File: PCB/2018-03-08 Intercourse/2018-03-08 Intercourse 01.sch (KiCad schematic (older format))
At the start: 47 parts, among them J1 USB_C_Receptacle, J2 TP_RST, J3 TP_TX, J4 TP_RX, J5 TP_GPIO0, J6 TP_GND1, J7 TP_GND2, J8 TP_GND3, U1 LTC3225, U2 TPS61221DCKR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

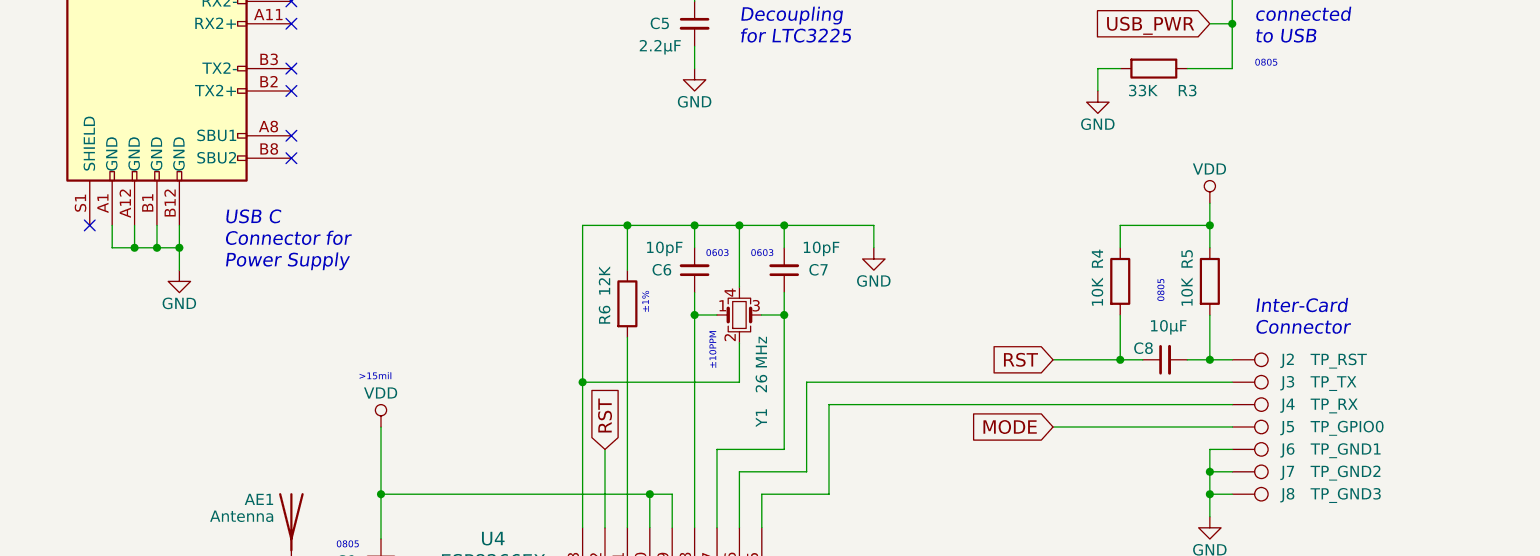
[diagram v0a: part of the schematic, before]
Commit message: Add USBRST Connection on .sch & .pcb
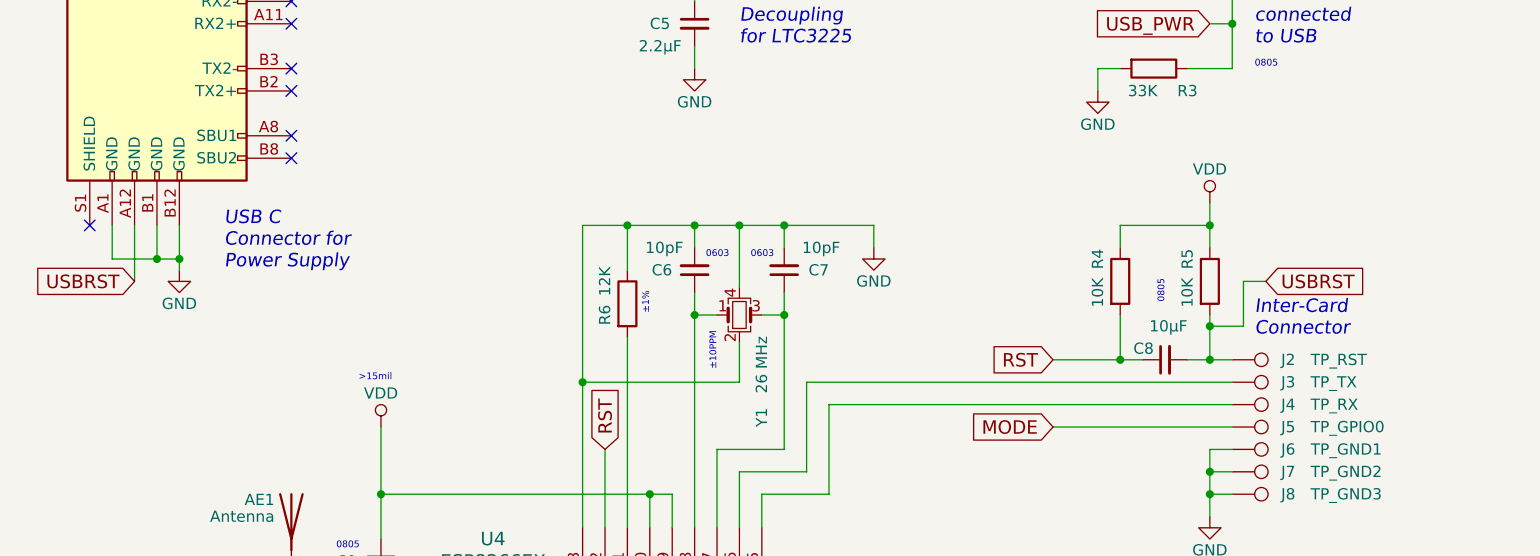
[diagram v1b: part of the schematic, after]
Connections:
- net GND: no longer J1.A12 (GND)
- net USBRST: now reaches C8.2, J2.1, R5.2
- net USBRST: now also J1.A12 (GND)

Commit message: rev3
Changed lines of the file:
@@
 NoConn ~ 2600 7000
 NoConn ~ 4750 6600
-Text Notes 6300 5300 0    60   Italic 0
+Text Notes 6300 5000 0    60   Italic 0
 Inter-Card\nConnector
 $Comp
@@
 	0    1    1    0
 $EndComp
-Text GLabel 6350 5050 2    60   Input ~ 0
+Text GLabel 6400 5200 2    60   Input ~ 0
 USBRST
 Wire Wire Line
@@
 	6200 6000 6100 6000
 Connection ~ 6100 6000
-Wire Wire Line
-	6100 5250 6250 5250
-Wire Wire Line
-	6250 5250 6250 5050
-Wire Wire Line
-	6250 5050 6350 5050
-Connection ~ 6100 5250
-Text GLabel 1300 5050 0    60   Input ~ 0
+Text GLabel 1300 5050 3    60   Input ~ 0
 USBRST
 Wire Wire Line
@@
 	1400 4800 1400 4950
 Connection ~ 1400 4950
+Wire Wire Line
+	6100 5300 6250 5300
+Wire Wire Line
+	6250 5300 6250 5200
+Wire Wire Line
+	6250 5200 6400 5200
+Connection ~ 6100 5300
 $EndSCHEMATC

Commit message: updated antenna design
board ready for revision
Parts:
- removed AE1: Antenna, MyAntennas:AN91445, symbol Antenna
- added AE1: Antenna_Dipole, MyAntennas:AN91445_47_mils, symbol Device:Antenna_Dipole
- C1: symbol DMF3 -> 2018-03-08-Intercourse-01-rescue:DMF3
- C10, C11, C12, C2, C3, C4, C5, C6, C7, C8, C9: symbol C_Small -> 2018-03-08-Intercourse-01-rescue:C_Small
- D1, D2, D3, D4, D5: symbol LED -> 2018-03-08-Intercourse-01-rescue:LED
- J1: symbol USB_C_Receptacle -> 2018-03-08-Intercourse-01-rescue:USB_C_Receptacle
- J2, J3, J4, J5, J6, J7, J8: symbol TEST_1P -> 2018-03-08-Intercourse-01-rescue:TEST_1P
- L1: symbol L -> 2018-03-08-Intercourse-01-rescue:L
- R1, R10, R11, R12, R8, R9: symbol R_Small -> 2018-03-08-Intercourse-01-rescue:R_Small
- R13, R14, R15, R2, R3, R4, R5, R6, R7: symbol R -> 2018-03-08-Intercourse-01-rescue:R
- U1: symbol LTC3225 -> 2018-03-08-Intercourse-01-rescue:LTC3225
- U2: symbol TPS61221DCKR -> 2018-03-08-Intercourse-01-rescue:TPS61221DCKR
- U3: symbol W25Q32FVSSIG -> 2018-03-08-Intercourse-01-rescue:W25Q32FVSSIG
- U4: symbol ESP8266EX -> 2018-03-08-Intercourse-01-rescue:ESP8266EX
- Y1: symbol Crystal_GND24_Small -> 2018-03-08-Intercourse-01-rescue:Crystal_GND24_Small
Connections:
- net GND: now also AE1.1
- net at U4.2 (LNA/ANT): now also C10.1; no longer C10.2
- new net: AE1.2, C10.2

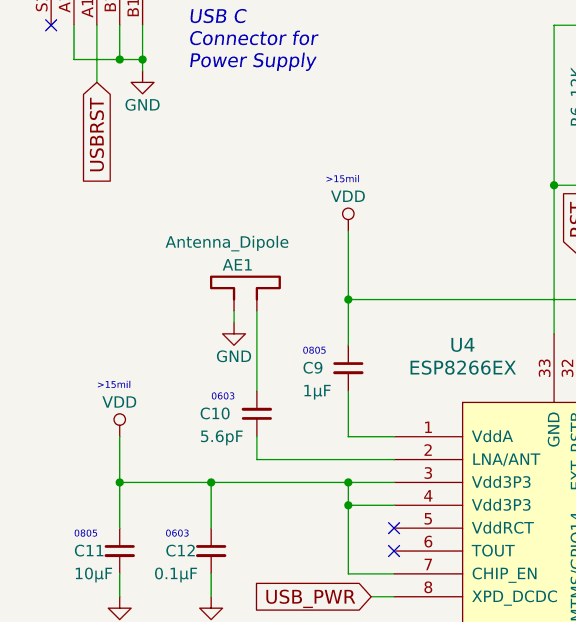
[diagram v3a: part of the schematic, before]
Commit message: rev4 ready for review
- added parts to antenna trace
- created gerber files
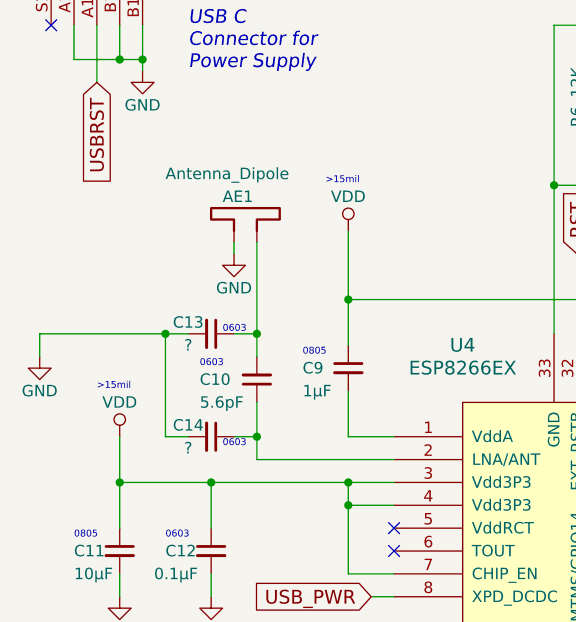
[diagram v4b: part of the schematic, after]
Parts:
- added C13, C14: ?, Capacitor_SMD:C_0603_1608Metric_Pad1.05x0.95mm_HandSolder, symbol Device:C_Small
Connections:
- net GND: now also C13.2, C14.2
- net at C10.1, U4.2 (LNA/ANT): now also C14.1
- net at AE1.2, C10.2: now also C13.1
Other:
- moved on the sheet: AE1, C10
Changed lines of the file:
@@
 L 2018-03-08-Intercourse-01-rescue:C_Small C10
 U 1 1 5AACE32B
-P 2000 6500
-F 0 "C10" H 1750 6500 50  0000 L CNN
-F 1 "5.6pF" H 1750 6600 50  0000 L CNN
-F 2 "Capacitors_SMD:C_0603_HandSoldering" H 2000 6500 50  0001 C CNN
-F 3 "" H 2000 6500 50  0001 C CNN
-	1    2000 6500
+P 2000 6350
+F 0 "C10" H 1750 6350 50  0000 L CNN
+F 1 "5.6pF" H 1750 6450 50  0000 L CNN
+F 2 "Capacitors_SMD:C_0603_HandSoldering" H 2000 6350 50  0001 C CNN
+F 3 "" H 2000 6350 50  0001 C CNN
+	1    2000 6350
 	1    0    0    1
 $EndComp
@@
 Text Notes 2200 6250 0    30   ~ 0
 0805
-Text Notes 1800 6450 0    30   ~ 0
+Text Notes 1750 6300 0    30   ~ 0
 0603\n
 Text Notes 1600 7050 0    30   ~ 0
@@
 	4100 8200 4100 7750
 Wire Wire Line
-	2000 6700 2000 6600
-Wire Wire Line
 	2000 6700 2600 6700
 Wire Wire Line
@@
 L 2018-03-08-Intercourse-01-rescue:GND #PWR0101
 U 1 1 5CF1DE7F
-P 1900 6100
-F 0 "#PWR0101" H 1900 5850 50  0001 C CNN
-F 1 "GND" H 1900 5950 50  0000 C CNN
-F 2 "" H 1900 6100 50  0001 C CNN
-F 3 "" H 1900 6100 50  0001 C CNN
-	1    1900 6100
+P 1900 5800
+F 0 "#PWR0101" H 1900 5550 50  0001 C CNN
+F 1 "GND" H 1900 5650 50  0000 C CNN
+F 2 "" H 1900 5800 50  0001 C CNN
+F 3 "" H 1900 5800 50  0001 C CNN
+	1    1900 5800
 	1    0    0    -1
 $EndComp
@@
 L Device:Antenna_Dipole AE1
 U 1 1 5CF1A8EB
-P 1900 5850
-F 0 "AE1" H 1850 5850 50  0000 L CNN
-F 1 "Antenna_Dipole" H 1600 5950 50  0000 L CNN
-F 2 "MyAntennas:AN91445_47_mils" H 1900 5850 50  0001 C CNN
-F 3 "~" H 1900 5850 50  0001 C CNN
-	1    1900 5850
-	1    0    0    -1
-$EndComp
-Wire Wire Line
-	2000 6400 2000 6050
-Wire Wire Line
-	1900 6050 1900 6100
+P 1900 5550
+F 0 "AE1" H 1850 5550 50  0000 L CNN
+F 1 "Antenna_Dipole" H 1600 5650 50  0000 L CNN
+F 2 "MyAntennas:AN91445_47_mils" H 1900 5550 50  0001 C CNN
+F 3 "~" H 1900 5550 50  0001 C CNN
+	1    1900 5550
+	1    0    0    -1
+$EndComp
+Wire Wire Line
+	1900 5750 1900 5800
+$Comp
+L Device:C_Small C14
+U 1 1 5CE7C39F
+P 1800 6600
+F 0 "C14" V 1750 6500 50  0000 C CNN
+F 1 "?" V 1850 6500 50  0000 C CNN
+F 2 "Capacitor_SMD:C_0603_1608Metric_Pad1.05x0.95mm_HandSolder" H 1800 6600 50  0001 C CNN
+F 3 "~" H 1800 6600 50  0001 C CNN
+	1    1800 6600
+	0    1    1    0
+$EndComp
+$Comp
+L Device:C_Small C13
+U 1 1 5CE8E238
+P 1800 6150
+F 0 "C13" V 1750 6050 50  0000 C CNN
+F 1 "?" V 1850 6050 50  0000 C CNN
+F 2 "Capacitor_SMD:C_0603_1608Metric_Pad1.05x0.95mm_HandSolder" H 1800 6150 50  0001 C CNN
+F 3 "~" H 1800 6150 50  0001 C CNN
+	1    1800 6150
+	0    1    1    0
+$EndComp
+Wire Wire Line
+	2000 5750 2000 6150
+Wire Wire Line
+	1900 6150 2000 6150
+Connection ~ 2000 6150
+Wire Wire Line
+	2000 6150 2000 6250
+Wire Wire Line
+	2000 6450 2000 6600
+Wire Wire Line
+	1900 6600 2000 6600
+Connection ~ 2000 6600
+Wire Wire Line
+	2000 6600 2000 6700
+Wire Wire Line
+	1700 6600 1600 6600
+Wire Wire Line
+	1600 6600 1600 6150
+Wire Wire Line
+	1600 6150 1700 6150
+$Comp
+L 2018-03-08-Intercourse-01-rescue:GND #PWR0102
+U 1 1 5CEE283A
+P 1050 6250
+F 0 "#PWR0102" H 1050 6000 50  0001 C CNN
+F 1 "GND" H 1050 6100 50  0000 C CNN
+F 2 "" H 1050 6250 50  0001 C CNN
+F 3 "" H 1050 6250 50  0001 C CNN
+	1    1050 6250
+	1    0    0    -1
+$EndComp
+Wire Wire Line
+	1600 6150 1050 6150
+Wire Wire Line
+	1050 6150 1050 6250
+Connection ~ 1600 6150
+Text Notes 1850 6150 0    30   ~ 0
+0603\n
+Text Notes 1850 6650 0    30   ~ 0
+0603\n
 $EndSCHEMATC
